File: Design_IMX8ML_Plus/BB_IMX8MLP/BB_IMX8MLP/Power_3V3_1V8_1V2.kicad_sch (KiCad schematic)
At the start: 32 parts, among them Q4 PMDT290UCE, U7 AOZ2261AQI-15

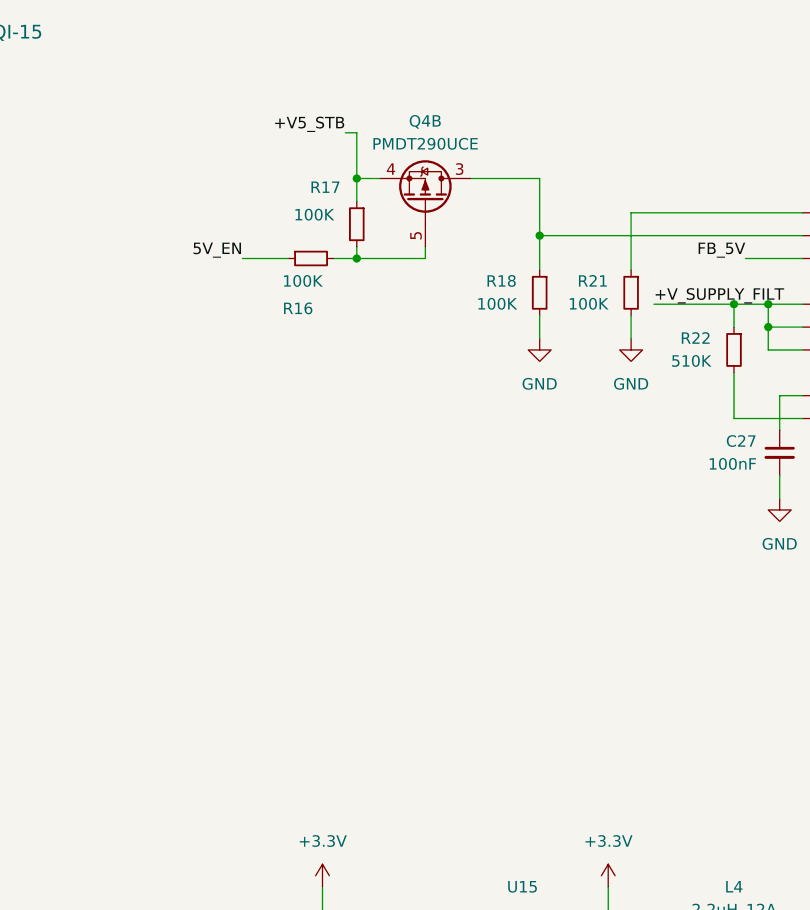
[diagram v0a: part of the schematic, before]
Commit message: reorganization of the componentes
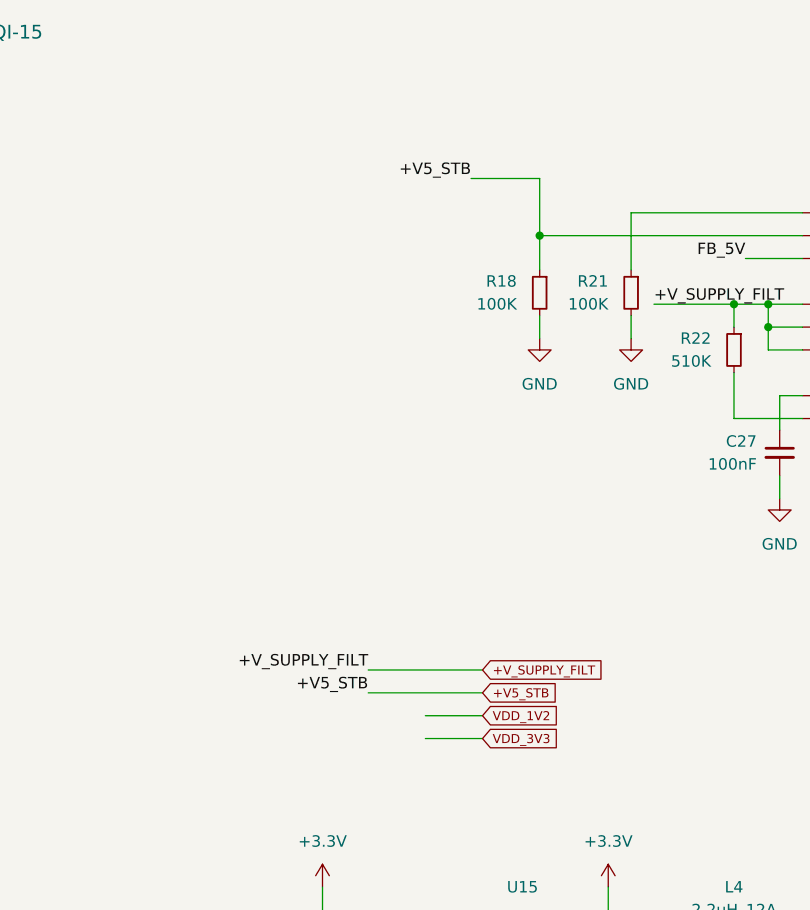
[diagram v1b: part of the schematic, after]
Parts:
- removed Q4: PMDT290UCE, Package_TO_SOT_SMD:SOT-666, symbol Transistor_FET:PMDT290UCE
- removed R16, R17: 100K, Resistor_SMD:R_0402_1005Metric, symbol Device:R_Small
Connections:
- net +V5_STB: now also R18.1, U7.2 (EN)

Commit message: pcb reorganization
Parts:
- L2: footprint Inductor_SMD:L_7.3x7.3_H3.5 -> _W_SBC:IND_PA4342.222NLT
- L3, L4: footprint Inductor_SMD:L_7.3x7.3_H3.5 -> _W_SBC:IND_SRP4020TA-1R0M_BRN
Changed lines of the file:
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@@
 			)
 		)
-		(property "Footprint" "Inductor_SMD:L_7.3x7.3_H3.5"
+		(property "Footprint" "_W_SBC:IND_SRP4020TA-1R0M_BRN"
 			(at 101.6 117.602 90)
 			(effects
@@
 			)
 		)
-		(property "Footprint" "Inductor_SMD:L_7.3x7.3_H3.5"
+		(property "Footprint" "_W_SBC:IND_PA4342.222NLT"
 			(at 113.03 40.64 0)
 			(effects
@@
 			)
 		)
-		(property "Footprint" "Inductor_SMD:L_7.3x7.3_H3.5"
+		(property "Footprint" "_W_SBC:IND_SRP4020TA-1R0M_BRN"
 			(at 222.25 116.332 90)
 			(effects

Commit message: CPU Board actualizate
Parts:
- U7: footprint _W_SBC:QFN4X4-22L_EP2_S_AOS -> QFN4X4-22L_EP2_S_AOS
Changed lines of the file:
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@@
 	)
 	(symbol
-		(lib_name "AOZ2261AQI-15_3")
 		(lib_id "AOZ2261AQI-15:AOZ2261AQI-15")
 		(at 234.95 48.26 0)
@@
 			)
 		)
-		(property "Footprint" "_W_SBC:QFN4X4-22L_EP2_S_AOS"
+		(property "Footprint" "QFN4X4-22L_EP2_S_AOS"
 			(at 234.95 48.26 0)
 			(effects
@@
 			)
 		)
-		(property "Footprint" "_W_SBC:QFN4X4-22L_EP2_S_AOS"
+		(property "Footprint" "QFN4X4-22L_EP2_S_AOS"
 			(at 128.27 38.1 0)
 			(effects

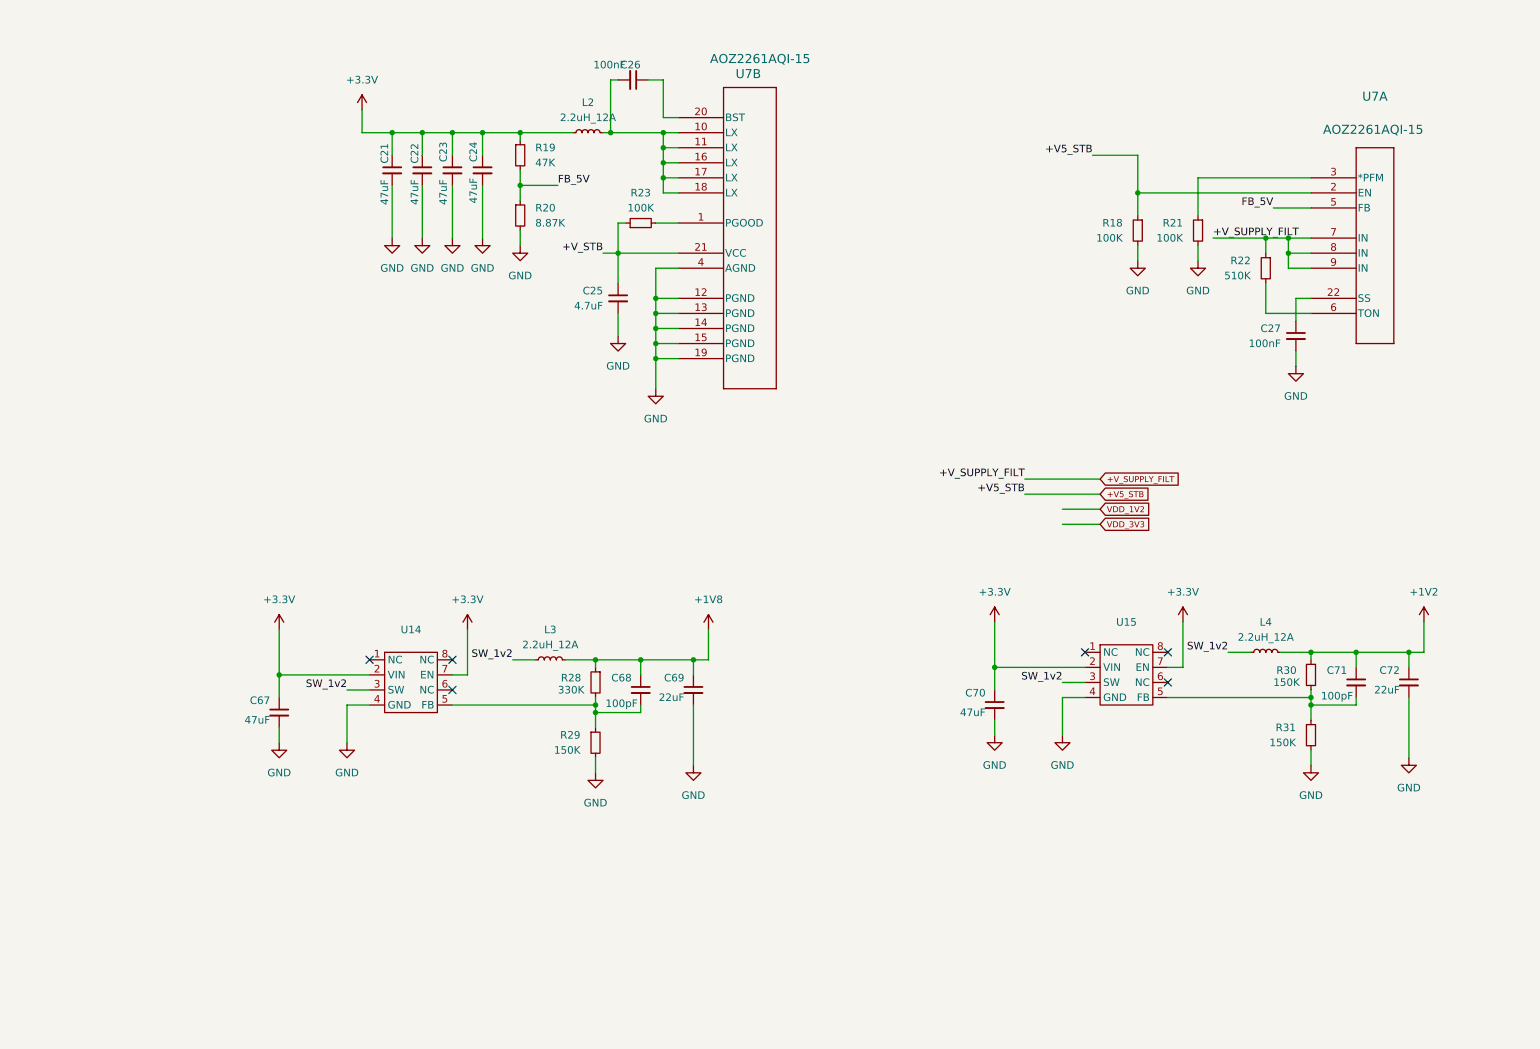
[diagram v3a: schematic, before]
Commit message: [BB_IMX8MLP IMX8MLP] Actuallizated to 9.0 kicad version
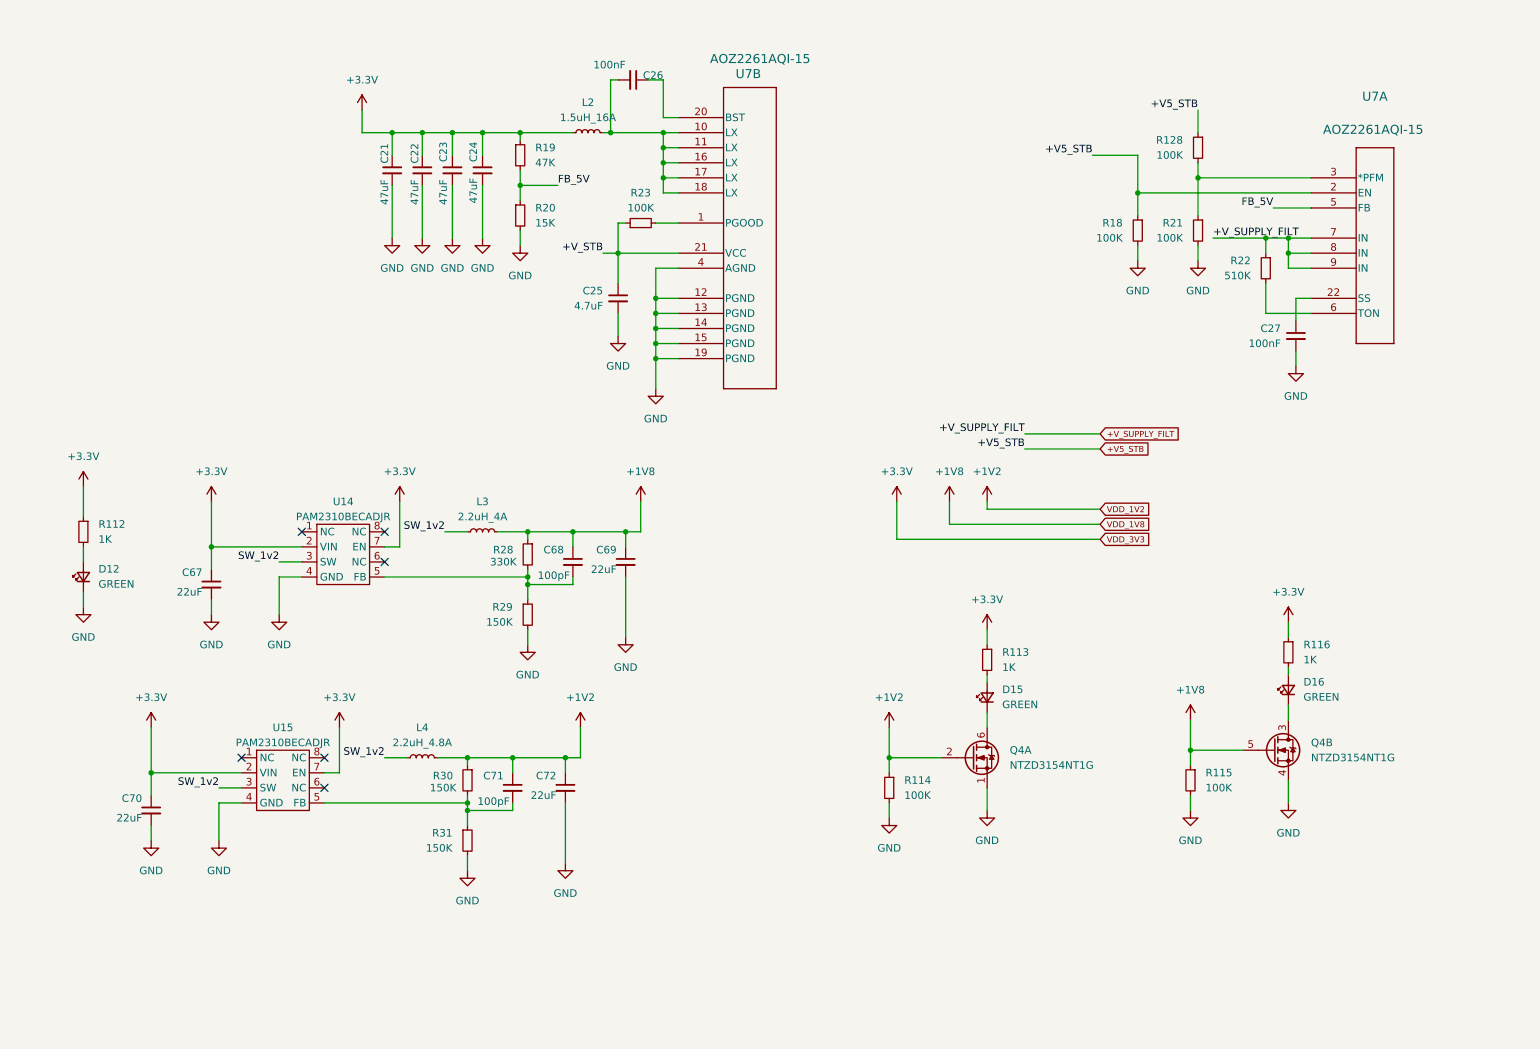
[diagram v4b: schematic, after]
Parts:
- added D12, D15, D16: GREEN, LED_SMD:LED_0402_1005Metric, symbol Device:LED_Small
- added Q4: NTZD3154NT1G, Package_TO_SOT_SMD:SOT-563, symbol Device:Q_Dual_NMOS_S1G1D2S2G2D1
- added R112, R113, R116: 1K, Resistor_SMD:R_0402_1005Metric, symbol Device:R_Small
- added R114, R115, R128: 100K, Resistor_SMD:R_0402_1005Metric, symbol Device:R_Small
- C21, C22, C23, C24, C69: footprint Capacitor_SMD:C_0402_1005Metric -> Capacitor_SMD:C_0805_2012Metric
- C25: footprint Capacitor_SMD:C_0402_1005Metric -> Capacitor_SMD:C_0603_1608Metric
- C26, C27: MP (none) -> C0402C104K4RACTU; Price (none) -> 0.1
- C67, C70: value 47uF -> 22uF; footprint Capacitor_SMD:C_0402_1005Metric -> Capacitor_SMD:C_0805_2012Metric
- C68, C71: MP (none) -> C0402C101K5RACTU; Price (none) -> 0.1
- L2: value 2.2uH_12A -> 1.5uH_16A; MP (none) -> PA4342.152NLT; Price (none) -> 1.5
- L3: value 2.2uH_12A -> 2.2uH_4A; MP (none) -> SRP4020TA-2R2M; Price (none) -> 1.5
- L4: value 2.2uH_12A -> 2.2uH_4.8A; MP (none) -> SRP4020TA-1R2M; Price (none) -> 1.5
- R18, R21, R23: MP (none) -> RC0402JR-07100KL; Price (none) -> 0.1
- R19: MP (none) -> RC0402FR-0747KL; Price (none) -> 0.1
- R20: value 8.87K -> 15K
- R22: MP (none) -> RMCF0402FT510K; Price (none) -> 0.1
- R28: MP (none) -> CRGCQ0402F330K; Price (none) -> 0.1
- R29, R30, R31: MP (none) -> RMCF0402FT150K; Price (none) -> 0.1
- U14: value ~ -> PAM2310BECADJR; MP (none) -> PAM2310BECADJR; Price (none) -> 0.75
- U15: value ~ -> PAM2310BECADJR
- U7: MP (none) -> AOZ2261AQI-15; Price (none) -> 1.5
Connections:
- net +1V2: now also Q4.2 (G), R114.1
- net +1V8: now also Q4.5 (G), R115.1
- net +3.3V: now also R112.1, R113.1, R116.1
- net +V5_STB: now also R128.1
- net GND: now also D12.1 (K), Q4.1 (S), Q4.4 (S), R114.2, R115.2
- net at R21.1, U7.3 (*PFM): now also R128.2
- new net: D15.1 (K), Q4.6 (D)
- new net: D16.2 (A), R116.2
- new net: D12.2 (A), R112.2
- new net: D16.1 (K), Q4.3 (D)
- new net: D15.2 (A), R113.2
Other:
- moved on the sheet: C67, C68, C69, C70, C71, C72, L3, L4, R28, R29, R30, R31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

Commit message: [LoRa] Starting a new project
Starting a new project base on LoRa LR1121, this project use
the module LBAA0XV2GT-001 that had sub-GHz and 2.4GHz frequencies.
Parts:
- C21, C22, C23, C24: MP (none) -> C2012X5R1A476M125AC; Price (none) -> 1
- U15: MP (none) -> PAM2310BECADJR; Price (none) -> 0.75
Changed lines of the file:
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@@
 			)
 		)
+		(property "MP" "C2012X5R1A476M125AC"
+			(at 85.09 46.99 90)
+			(effects
+				(font
+					(size 1.27 1.27)
+				)
+				(hide yes)
+			)
+		)
+		(property "Price" "1"
+			(at 85.09 46.99 90)
+			(effects
+				(font
+					(size 1.27 1.27)
+				)
+				(hide yes)
+			)
+		)
 		(pin "2"
 		)
@@
 			)
 		)
+		(property "MP" "C2012X5R1A476M125AC"
+			(at 90.17 46.99 90)
+			(effects
+				(font
+					(size 1.27 1.27)
+				)
+				(hide yes)
+			)
+		)
+		(property "Price" "1"
+			(at 90.17 46.99 90)
+			(effects
+				(font
+					(size 1.27 1.27)
+				)
+				(hide yes)
+			)
+		)
 		(pin "2"
 		)
@@
 			)
 		)
+		(property "MP" "PAM2310BECADJR"
+			(at 60.96 144.78 0)
+			(effects
+				(font
+					(size 1.27 1.27)
+				)
+				(hide yes)
+			)
+		)
+		(property "Price" "0.75"
+			(at 60.96 144.78 0)
+			(effects
+				(font
+					(size 1.27 1.27)
+				)
+				(hide yes)
+			)
+		)
 		(pin "6"
 		)
@@
 			)
 		)
+		(property "MP" "C2012X5R1A476M125AC"
+			(at 80.01 46.99 90)
+			(effects
+				(font
+					(size 1.27 1.27)
+				)
+				(hide yes)
+			)
+		)
+		(property "Price" "1"
+			(at 80.01 46.99 90)
+			(effects
+				(font
+					(size 1.27 1.27)
+				)
+				(hide yes)
+			)
+		)
 		(pin "2"
 		)
@@
 			(at 95.25 46.99 90)
 			(effects
+				(font
+					(size 1.27 1.27)
+				)
+				(hide yes)
+			)
+		)
+		(property "MP" "C2012X5R1A476M125AC"
+			(at 95.25 46.99 90)
+			(effects
+				(font
+					(size 1.27 1.27)
+				)
+				(hide yes)
+			)
+		)
+		(property "Price" "1"
+			(at 95.25 46.99 90)
+			(effects

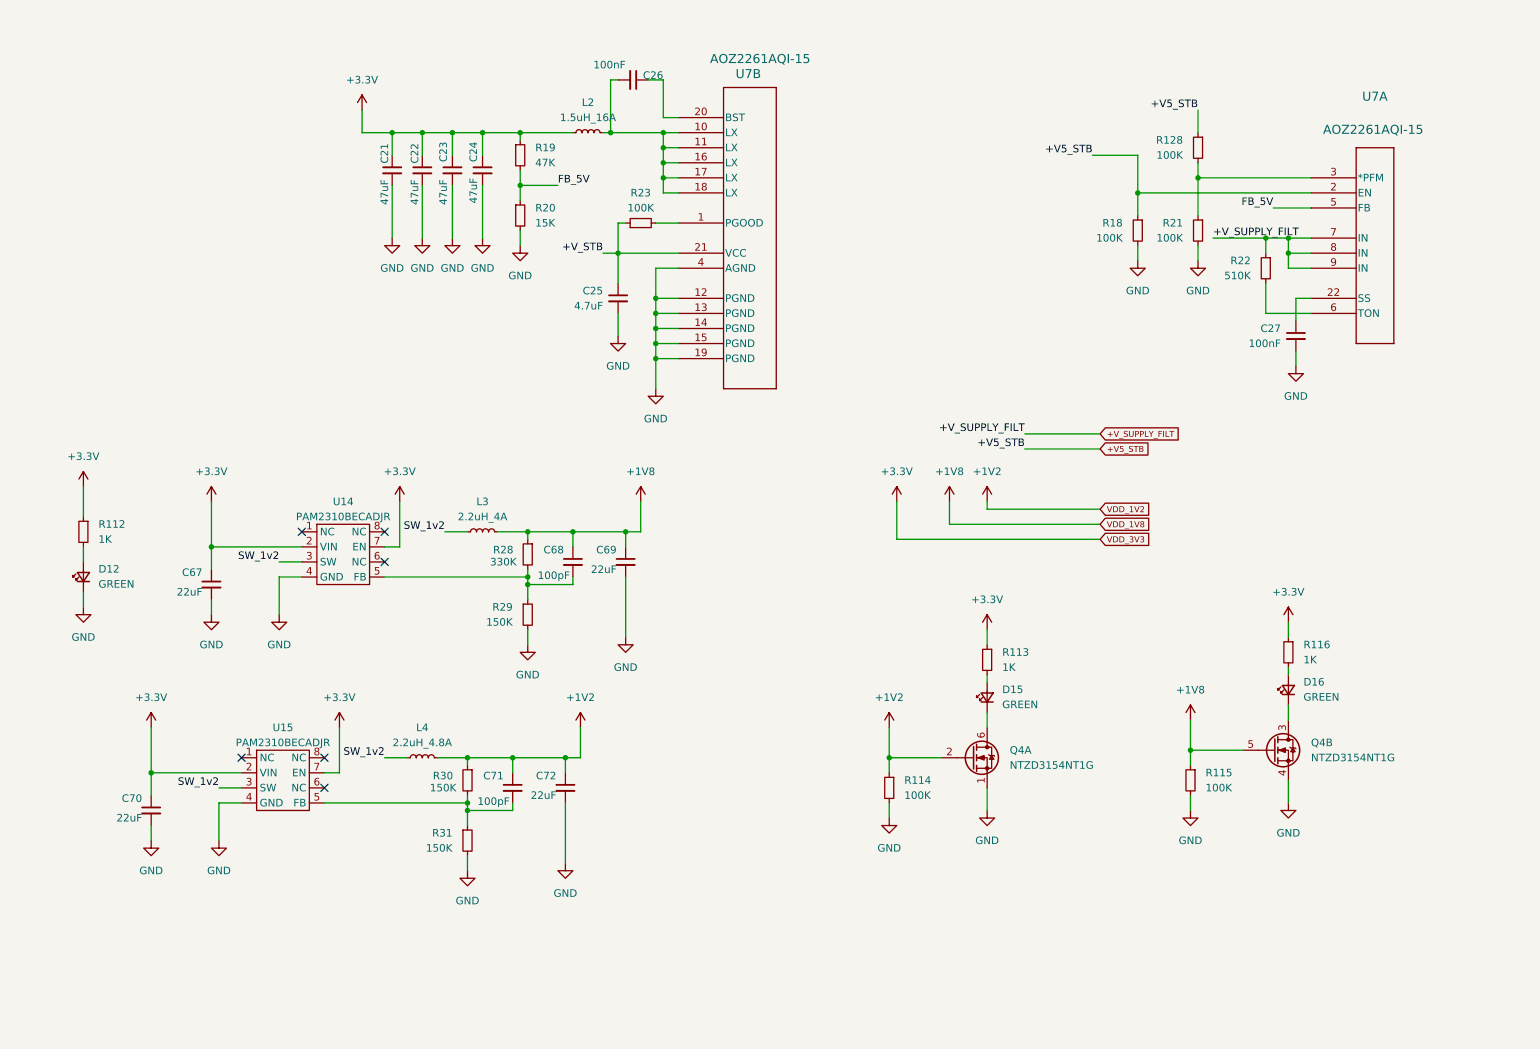
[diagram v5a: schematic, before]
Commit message: [BB_IMX8ML] It was reoganizated the device position
It was reorganized the devices to improve the routing.
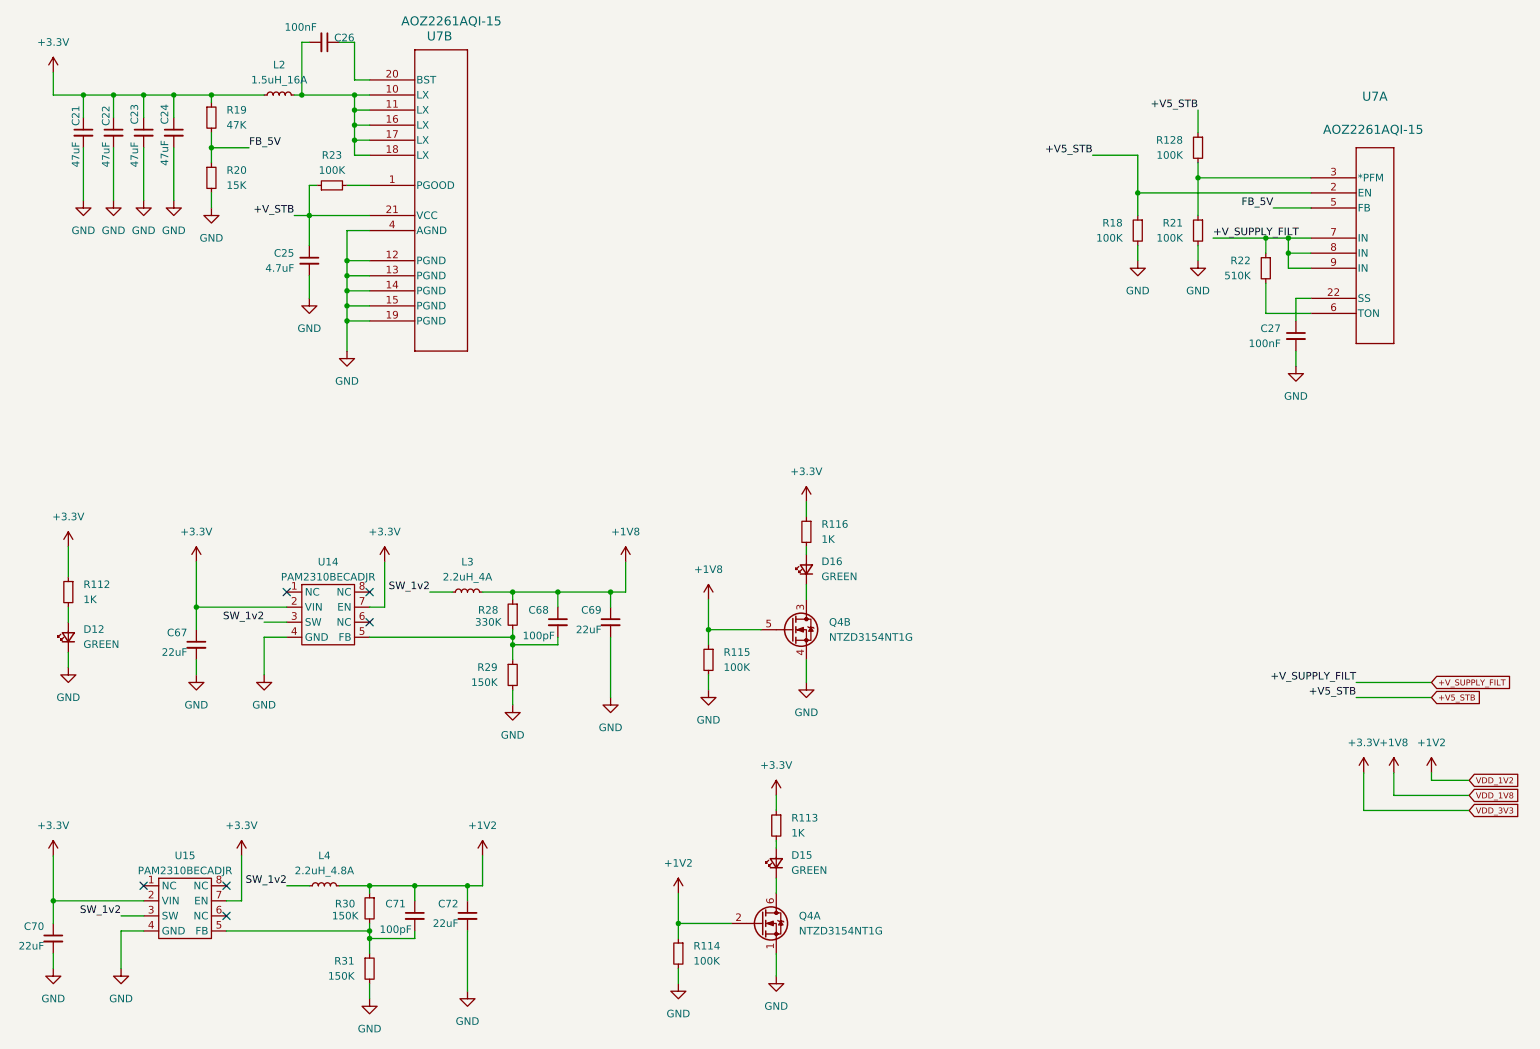
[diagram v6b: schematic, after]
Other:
- moved on the sheet: C21, C22, C23, C24, C25, C26, C67, C68, C69, C70, C71, C72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
